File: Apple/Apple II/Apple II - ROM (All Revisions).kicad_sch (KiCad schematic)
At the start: 0 parts

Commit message: Finished Apple II - Sheet 10 - ROM (all revisions)
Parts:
- added F12: 74LS138, symbol Apple II:F12_74LS138
- added H1: 74LS08, symbol Apple II:H1_74LS08
- added N1: 1, symbol Apple II:NOTE_NUMBER
- added N2: 2, symbol Apple II:NOTE_NUMBER
- added RA01: 1K, Resistor_THT:R_Array_SIP9, symbol Apple II:R_Network08_US_Split
- added U?: 9316B_ROM_ARRAY, symbol Apple II:9316B_ROM_ARRAY
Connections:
- new net: F12.10 (~{Z5}), U?.20 (~{CS1}), U?.21 (~{CS3})
- new net: F12.11 (~{Z4}), U?.20 (~{CS1}), U?.21 (~{CS3})
- new net: F12.12 (~{Z3}), U?.20 (~{CS1}), U?.21 (~{CS3})
- new net: F12.13 (~{Z2}), U?.20 (~{CS1}), U?.21 (~{CS3})
- new net: F12.6 (E3), H1.6
- new net: F12.7 (~{Z7}), U?.20 (~{CS1}), U?.21 (~{CS3})
- new net: F12.9 (~{Z6}), U?.20 (~{CS1}), U?.21 (~{CS3})
- new net +5V: RA01.1 (R1.1)
- new net AD0_{2}: U?.8 (A0)
- new net AD10_{12}: U?.19 (A10)
- new net AD11_{13}: F12.1 (A0)
- new net AD12_{14}: F12.2 (A1)
- new net AD13_{15}: F12.3 (A2)
- new net AD14_{16}: H1.4
- new net AD15_{17}: H1.5
- new net AD1_{3}: U?.7 (A1)
- new net AD2_{4}: U?.6 (A2)
- new net AD3_{5}: U?.5 (A3)
- new net AD4_{6}: U?.4 (A4)
- new net AD5_{7}: U?.3 (A5)
- new net AD6_{8}: U?.2 (A6)
- new net AD7_{9}: U?.1 (A7)
- new net AD8_{10}: U?.23 (A8)
- new net AD9_{11}: U?.22 (A9)
- new net D0_{49}: U?.9 (D0)
- new net D1_{48}: U?.10 (D1)
- new net D2_{47}: U?.11 (D2)
- new net D3_{46}: U?.13 (D3)
- new net D4_{45}: U?.14 (D4)
- new net D5_{46}: U?.15 (D5)
- new net D6_{47}: U?.16 (D6)
- new net D7_{48}: U?.17 (D7)
- new net F12-15: F12.15 (~{Z0})
- new net ~{INH}_{32}: RA01.7 (R6.2), U?.18 (CS2)
- new net ~{I/O STB}_{20}: F12.14 (~{Z1})
- new net ɸ1_{38}: F12.4 (~{E1}), F12.5 (~{E2})
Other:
- note added: "ADDRESS"
- note added: "FROM CLOCK GENERATOR"
- note added: "FROM MICROPROCESOR"
- note added: "FROM PERIPHERAL I/O"
- note added: "MOTHERBOARD LOCATION"
- note added: "TO MICROPROCESSOR"
- note added: "TO PERIPHERAL I/O"
- title: (none) -> Apple II - ROM

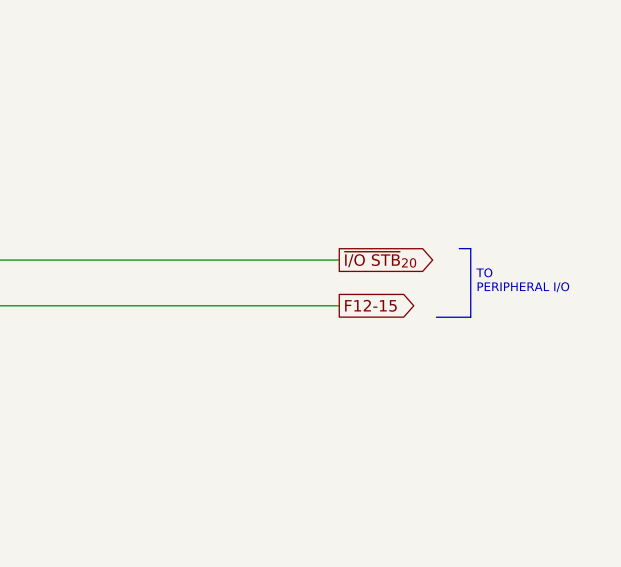
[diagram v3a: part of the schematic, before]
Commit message: Finished Apple II - Sheet 11 - Peripheral I/O (all revisions)
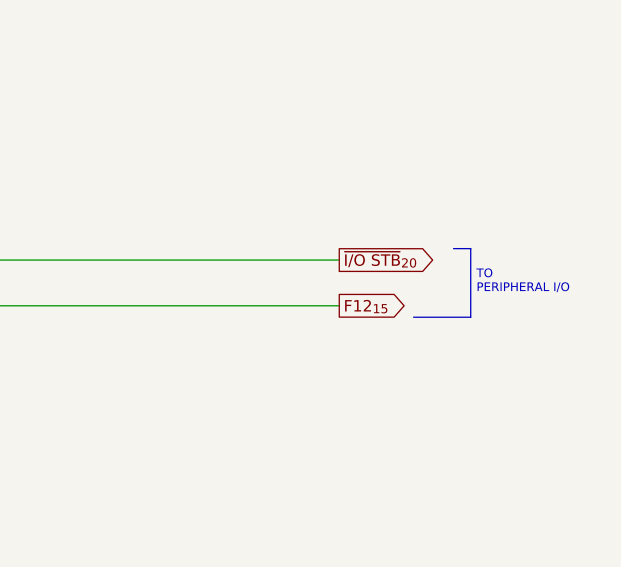
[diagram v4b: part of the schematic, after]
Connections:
- net at U?.20 (~{CS1}), U?.21 (~{CS3}): now also F12.9 (~{Z6}); no longer F12.10 (~{Z5})
- net F12-15 renamed F12_{15}
- new net: F12.10 (~{Z5}), U?.20 (~{CS1}), U?.21 (~{CS3})
- new net: F12.11 (~{Z4}), U?.20 (~{CS1}), U?.21 (~{CS3})
- new net: F12.12 (~{Z3}), U?.20 (~{CS1}), U?.21 (~{CS3})
- new net: F12.13 (~{Z2}), U?.20 (~{CS1}), U?.21 (~{CS3})
- new net: F12.7 (~{Z7}), U?.20 (~{CS1}), U?.21 (~{CS3})
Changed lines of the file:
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@@
     (stroke (width 0) (type default) (color 0 0 0 0))
   )
-  (polyline (pts (xy 354.965 181.61) (xy 356.235 181.61))
+  (polyline (pts (xy 354.33 181.61) (xy 356.235 181.61))
     (stroke (width 0) (type solid) (color 0 0 0 0))
   )
@@
     (stroke (width 0) (type default) (color 0 0 0 0))
   )
-  (polyline (pts (xy 352.425 189.23) (xy 356.235 189.23))
+  (polyline (pts (xy 349.885 189.23) (xy 356.235 189.23))
     (stroke (width 0) (type solid) (color 0 0 0 0))
   )
@@
     )
   )
-  (global_label "F12-15" (shape output) (at 341.63 187.96 0) (fields_autoplaced)
-    (effects (font (size 1.27 1.27)) (justify left))
-    (property "Intersheet References" "${INTERSHEET_REFS}" (id 0) (at 351.5421 187.8806 0)
-      (effects (font (size 1.27 1.27)) (justify left) hide)
-    )
+  (global_label "F12_{15}" (shape output) (at 341.63 187.96 0) (fields_autoplaced)
+    (effects (font (size 1.27 1.27)) (justify left))
+    (property "Intersheet References" "${INTERSHEET_REFS}" (id 0) (at 349.486 187.8806 0)
+      (effects (font (size 1.27 1.27)) (justify left) hide)
+    )

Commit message: Finished Apple II - Sheet 14 - Video Generator Part 1 (Rev 0)
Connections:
- net at U?.20 (~{CS1}), U?.21 (~{CS3}): now also F12.9 (~{Z6}); no longer F12.10 (~{Z5})
- new net: F12.10 (~{Z5}), U?.20 (~{CS1}), U?.21 (~{CS3})
- new net: F12.11 (~{Z4}), U?.20 (~{CS1}), U?.21 (~{CS3})
- new net: F12.12 (~{Z3}), U?.20 (~{CS1}), U?.21 (~{CS3})
- new net: F12.13 (~{Z2}), U?.20 (~{CS1}), U?.21 (~{CS3})
- new net: F12.7 (~{Z7}), U?.20 (~{CS1}), U?.21 (~{CS3})

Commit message: Finished Apple II - Sheet 20 - Video Generator Part 2 (Rev RFI)
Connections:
- net at U?.20 (~{CS1}), U?.21 (~{CS3}): now also F12.9 (~{Z6}); no longer F12.10 (~{Z5})
- new net: F12.10 (~{Z5}), U?.20 (~{CS1}), U?.21 (~{CS3})
- new net: F12.11 (~{Z4}), U?.20 (~{CS1}), U?.21 (~{CS3})
- new net: F12.12 (~{Z3}), U?.20 (~{CS1}), U?.21 (~{CS3})
- new net: F12.13 (~{Z2}), U?.20 (~{CS1}), U?.21 (~{CS3})
- new net: F12.7 (~{Z7}), U?.20 (~{CS1}), U?.21 (~{CS3})

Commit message: Finished Apple II - Single Piece Keyboard
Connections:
- net at U?.20 (~{CS1}), U?.21 (~{CS3}): now also F12.9 (~{Z6}); no longer F12.10 (~{Z5})
- new net: F12.10 (~{Z5}), U?.20 (~{CS1}), U?.21 (~{CS3})
- new net: F12.11 (~{Z4}), U?.20 (~{CS1}), U?.21 (~{CS3})
- new net: F12.12 (~{Z3}), U?.20 (~{CS1}), U?.21 (~{CS3})
- new net: F12.13 (~{Z2}), U?.20 (~{CS1}), U?.21 (~{CS3})
- new net: F12.7 (~{Z7}), U?.20 (~{CS1}), U?.21 (~{CS3})

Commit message: Finished Apple II - Sheet 22 - Two-Piece Keyboard
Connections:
- net at U?.20 (~{CS1}), U?.21 (~{CS3}): now also F12.9 (~{Z6}); no longer F12.10 (~{Z5})
- new net: F12.10 (~{Z5}), U?.20 (~{CS1}), U?.21 (~{CS3})
- new net: F12.11 (~{Z4}), U?.20 (~{CS1}), U?.21 (~{CS3})
- new net: F12.12 (~{Z3}), U?.20 (~{CS1}), U?.21 (~{CS3})
- new net: F12.13 (~{Z2}), U?.20 (~{CS1}), U?.21 (~{CS3})
- new net: F12.7 (~{Z7}), U?.20 (~{CS1}), U?.21 (~{CS3})
